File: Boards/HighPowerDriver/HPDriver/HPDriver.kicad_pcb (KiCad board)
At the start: 4 copper layers, 100.6 x 76.2 mm, 143 parts, among them J1 60V_In, J2 USB_B_Mini, J3 Coils, J4 Screw_Terminal_01x06, J5 AVR-ISP-6, Q1 IRFR5410, Q10 IRF4950S, Q11 BC817, Q12 BC817, Q13 BC817, Q14 BC817, Q2 IRFR3910, Q3 IRFR3910, Q4 IRFR5410, Q5 IRFR5410, Q6 IRFR3910, Q7 IRFR3910, Q8 IRFR5410, Q9 BC817, SW1 SW_Push, U1 LM5009MM, U10 ATtiny2313A-SU, U11 74LVC1G125, U12 74LVC1G125, U13 74AHC1G00, U14 74LVC1G123, U2 TMC262, U3 FT230XS, U4 SFH6156, U5 SFH6156, U6 TLP118, U7 LTV-827S, U8 LTV-827S, U9 74HC14, X1 16MHz, Y1 20MHz

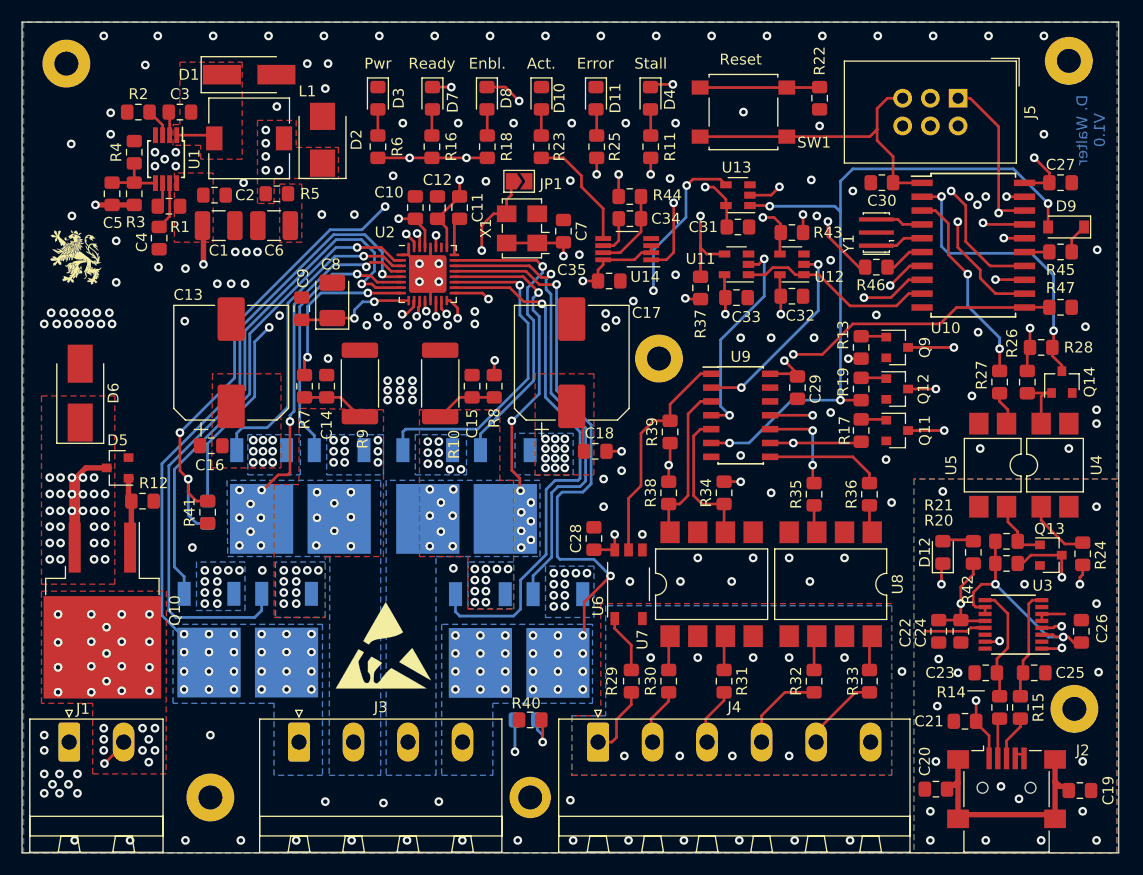
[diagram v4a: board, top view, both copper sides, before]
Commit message: Added Logic to allow local control of stepper trough µC
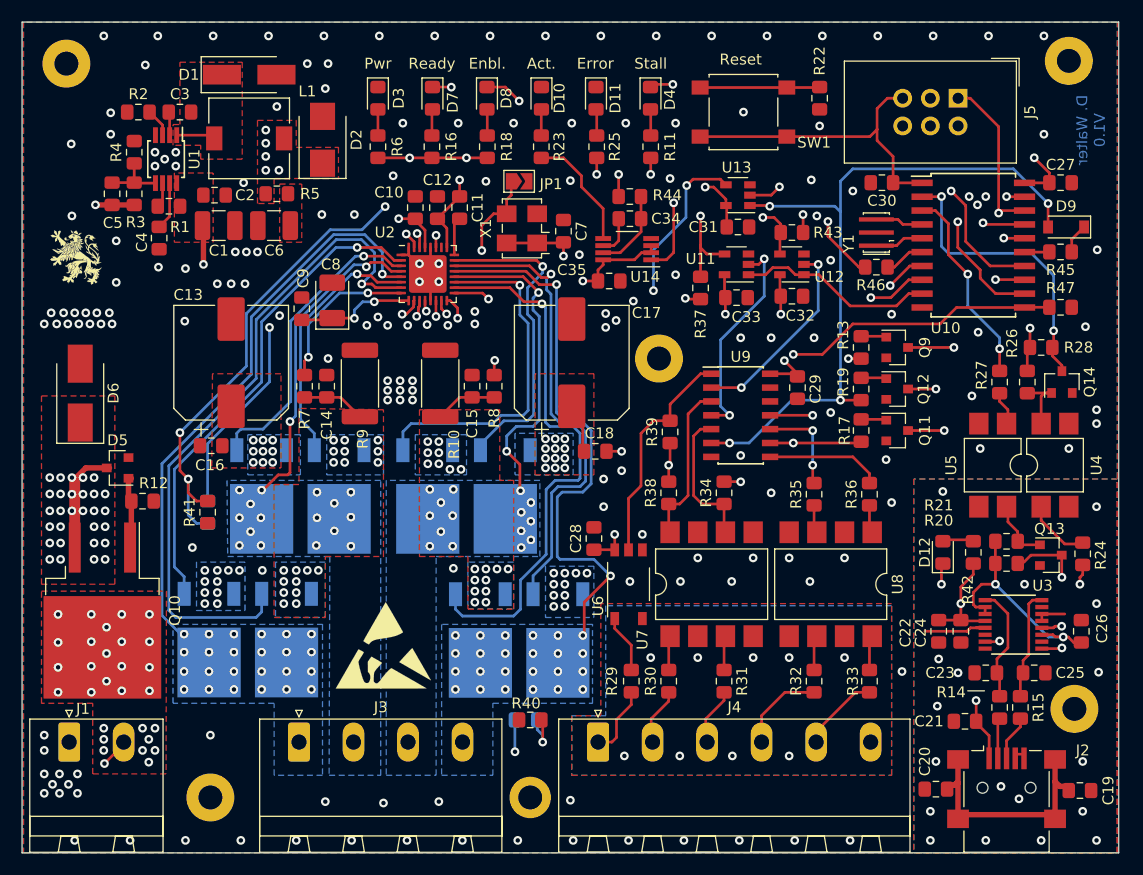
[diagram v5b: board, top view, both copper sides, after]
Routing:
- net Net-(Q7-Pad1): track 30.2 -> 31.9 mm
- net Net-(R43-Pad2): track 19.6 -> 17.9 mm
- net Net-(Q8-Pad1): track 28.0 -> 29.3 mm
- net Net-(Q1-Pad1): track 29.3 -> 28.0 mm
- net /Connector/Coil_B1: track 28.3 -> 29.6 mm
- net Net-(Q3-Pad1): track 49.6 -> 50.7 mm
- net Net-(Q2-Pad1): track 24.6 -> 23.5 mm
- net /Connector/Coil_A2: track 30.8 -> 29.7 mm
- net Net-(R7-Pad2): track 15.5 -> 14.5 mm
- net /Connector/Coil_B2: track 51.0 -> 51.9 mm
- net Net-(Q4-Pad1): track 43.7 -> 44.5 mm
- net Net-(C14-Pad1): track 6.61 -> 5.81 mm
- net +5V: track 92.8 -> 92.0 mm

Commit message: Changed Controller to ATtiny406
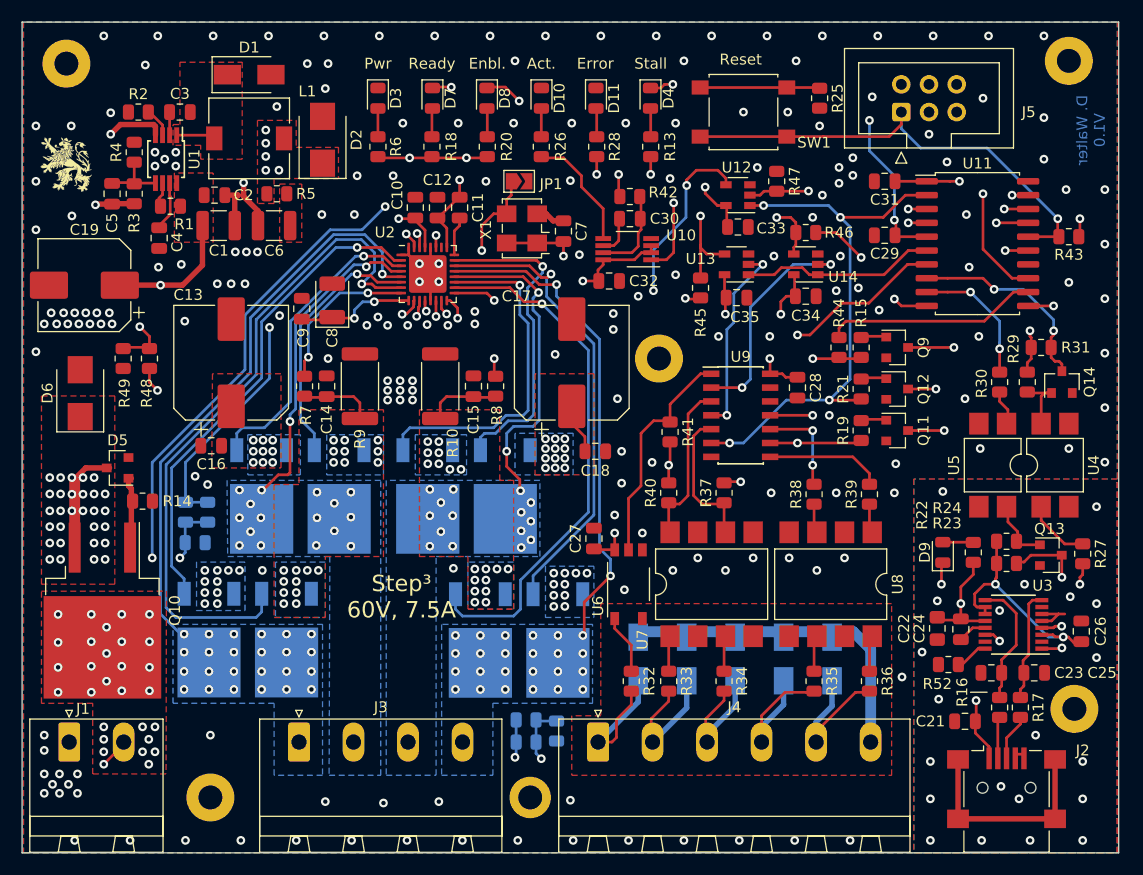
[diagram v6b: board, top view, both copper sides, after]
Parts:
- removed C20: 10nF, Capacitor_SMD:C_0805_2012Metric_Pad1.15x1.40mm_HandSolder
- removed the C30 at (163.2, 79.5)
- removed the D9 at (180.1, 83.6)
- removed the R45 at (179.6, 85.9)
- removed the REF** at (117.5, 121.9)
- removed the REF** at (99.7, 71.1)
- removed the U10 at (171.6, 85.2)
- removed Y1: 20MHz, Crystal:Resonator_SMD_muRata_CSTxExxV-3Pin_3.0x1.1mm_HandSoldering
- added C29: 470nF, Capacitor_SMD:C_0805_2012Metric, F.Cu at (163.4, 84.3)
- added D12: 13V, Diode_SMD:D_SMA, B.Cu at (140.8, 123.2)
- added D13: 13V, Diode_SMD:D_SMA, B.Cu at (145.3, 123.2)
- added D14: 13V, Diode_SMD:D_SMA, B.Cu at (149.7, 123.2)
- added D15: 13V, Diode_SMD:D_SMA, B.Cu at (154.2, 123.2)
- added D16: 13V, Diode_SMD:D_SMA, B.Cu at (158.6, 123.2)
- added R43: 10k, Resistor_SMD:R_0805_2012Metric, F.Cu at (180.3, 84.5)
- added R48: 10k, Resistor_SMD:R_0805_2012Metric, F.Cu at (96.0, 95.6)
- added R49: 750R, Resistor_SMD:R_0805_2012Metric, F.Cu at (93.6, 95.6)
- added R50: 39k, Resistor_SMD:R_0805_2012Metric, B.Cu at (99.3, 109.7)
- added R51: 39k, Resistor_SMD:R_0805_2012Metric, B.Cu at (130.6, 130.8)
- added R52: 1k, Resistor_SMD:R_0805_2012Metric, F.Cu at (169.3, 123.7)
- added U11: ATtiny406-S, Package_SO:SOIC-20W_7.5x12.8mm_P1.27mm, F.Cu at (172.0, 85.1)
- C1, C6: footprint Capacitor_SMD:C_1210_3225Metric_Pad1.42x2.65mm_HandSolder -> Capacitor_SMD:C_1210_3225Metric
- C10, C11, C12, C14, C15, C16, C18, C2, C21, C23, C24, C25, C26, C3, C4, C5, C7, C9: footprint Capacitor_SMD:C_0805_2012Metric_Pad1.15x1.40mm_HandSolder -> Capacitor_SMD:C_0805_2012Metric
- C19: value 10nF -> 47µF/100V; footprint Capacitor_SMD:C_0805_2012Metric_Pad1.15x1.40mm_HandSolder -> Capacitor_SMD:CP_Elec_8x10
- C27: renamed from C28; footprint Capacitor_SMD:C_0805_2012Metric_Pad1.15x1.40mm_HandSolder -> Capacitor_SMD:C_0805_2012Metric
- C28: renamed from C29; footprint Capacitor_SMD:C_0805_2012Metric_Pad1.15x1.40mm_HandSolder -> Capacitor_SMD:C_0805_2012Metric
- C30: renamed from C34; footprint Capacitor_SMD:C_0805_2012Metric_Pad1.15x1.40mm_HandSolder -> Capacitor_SMD:C_0805_2012Metric
- C31: renamed from C27; footprint Capacitor_SMD:C_0805_2012Metric_Pad1.15x1.40mm_HandSolder -> Capacitor_SMD:C_0805_2012Metric
- C32: renamed from C35; footprint Capacitor_SMD:C_0805_2012Metric_Pad1.15x1.40mm_HandSolder -> Capacitor_SMD:C_0805_2012Metric
- C33: renamed from C31; footprint Capacitor_SMD:C_0805_2012Metric_Pad1.15x1.40mm_HandSolder -> Capacitor_SMD:C_0805_2012Metric
- C34: renamed from C32; footprint Capacitor_SMD:C_0805_2012Metric_Pad1.15x1.40mm_HandSolder -> Capacitor_SMD:C_0805_2012Metric
- C35: renamed from C33; footprint Capacitor_SMD:C_0805_2012Metric_Pad1.15x1.40mm_HandSolder -> Capacitor_SMD:C_0805_2012Metric
- C8: footprint Capacitor_Tantalum_SMD:CP_EIA-3528-21_Kemet-B_Pad1.50x2.35mm_HandSolder -> Capacitor_Tantalum_SMD:CP_EIA-3528-21_Kemet-B
- D1: footprint Diode_SMD:D_SMA_Handsoldering -> Diode_SMD:D_SMA
- D10, D11, D3, D4, D7, D8: footprint LED_SMD:LED_0805_2012Metric_Pad1.15x1.40mm_HandSolder -> LED_SMD:LED_0805_2012Metric
- D6: value D_TVS -> 64V; footprint Diode_SMD:D_SMB_Handsoldering -> Diode_SMD:D_SMB
- D9: renamed from D12; footprint LED_SMD:LED_0805_2012Metric_Pad1.15x1.40mm_HandSolder -> LED_SMD:LED_0805_2012Metric
- J4: value Screw_Terminal_01x06 -> Control
- J5: value AVR-ISP-6 -> AVR-UPDI-6
- R1, R2, R3, R4, R47, R5, R6, R7, R8: footprint Resistor_SMD:R_0805_2012Metric_Pad1.15x1.40mm_HandSolder -> Resistor_SMD:R_0805_2012Metric
- R10, R9: footprint Resistor_SMD:R_2512_6332Metric_Pad1.40x3.35mm_HandSolder -> Resistor_SMD:R_2512_6332Metric
- R11: renamed from R40; value R -> 3k9; footprint Resistor_SMD:R_0805_2012Metric_Pad1.15x1.40mm_HandSolder -> Resistor_SMD:R_0805_2012Metric; moved to B.Cu
- R12: renamed from R41; value R -> 3k9; footprint Resistor_SMD:R_0805_2012Metric_Pad1.15x1.40mm_HandSolder -> Resistor_SMD:R_0805_2012Metric; moved to B.Cu
- R13: renamed from R11; footprint Resistor_SMD:R_0805_2012Metric_Pad1.15x1.40mm_HandSolder -> Resistor_SMD:R_0805_2012Metric
- R14: renamed from R12; footprint Resistor_SMD:R_0805_2012Metric_Pad1.15x1.40mm_HandSolder -> Resistor_SMD:R_0805_2012Metric
- R15: renamed from R13; footprint Resistor_SMD:R_0805_2012Metric_Pad1.15x1.40mm_HandSolder -> Resistor_SMD:R_0805_2012Metric
- R16: renamed from R14; footprint Resistor_SMD:R_0805_2012Metric_Pad1.15x1.40mm_HandSolder -> Resistor_SMD:R_0805_2012Metric
- R17: renamed from R15; footprint Resistor_SMD:R_0805_2012Metric_Pad1.15x1.40mm_HandSolder -> Resistor_SMD:R_0805_2012Metric
- R18: renamed from R16; footprint Resistor_SMD:R_0805_2012Metric_Pad1.15x1.40mm_HandSolder -> Resistor_SMD:R_0805_2012Metric
- R19: renamed from R17; footprint Resistor_SMD:R_0805_2012Metric_Pad1.15x1.40mm_HandSolder -> Resistor_SMD:R_0805_2012Metric
- R20: renamed from R18; footprint Resistor_SMD:R_0805_2012Metric_Pad1.15x1.40mm_HandSolder -> Resistor_SMD:R_0805_2012Metric
- R21: renamed from R19; footprint Resistor_SMD:R_0805_2012Metric_Pad1.15x1.40mm_HandSolder -> Resistor_SMD:R_0805_2012Metric
- R22: renamed from R42; footprint Resistor_SMD:R_0805_2012Metric_Pad1.15x1.40mm_HandSolder -> Resistor_SMD:R_0805_2012Metric
- R23: renamed from R20; footprint Resistor_SMD:R_0805_2012Metric_Pad1.15x1.40mm_HandSolder -> Resistor_SMD:R_0805_2012Metric
- R24: renamed from R21; footprint Resistor_SMD:R_0805_2012Metric_Pad1.15x1.40mm_HandSolder -> Resistor_SMD:R_0805_2012Metric
- R25: renamed from R22; value 1k -> 330R; footprint Resistor_SMD:R_0805_2012Metric_Pad1.15x1.40mm_HandSolder -> Resistor_SMD:R_0805_2012Metric
- R26: renamed from R23; footprint Resistor_SMD:R_0805_2012Metric_Pad1.15x1.40mm_HandSolder -> Resistor_SMD:R_0805_2012Metric
- R27: renamed from R24; value 380R -> 200R; footprint Resistor_SMD:R_0805_2012Metric_Pad1.15x1.40mm_HandSolder -> Resistor_SMD:R_0805_2012Metric
- R28: renamed from R25; footprint Resistor_SMD:R_0805_2012Metric_Pad1.15x1.40mm_HandSolder -> Resistor_SMD:R_0805_2012Metric
- R29: renamed from R26; footprint Resistor_SMD:R_0805_2012Metric_Pad1.15x1.40mm_HandSolder -> Resistor_SMD:R_0805_2012Metric
- R30: renamed from R27; value 380R -> 200R; footprint Resistor_SMD:R_0805_2012Metric_Pad1.15x1.40mm_HandSolder -> Resistor_SMD:R_0805_2012Metric
- R31: renamed from R28; footprint Resistor_SMD:R_0805_2012Metric_Pad1.15x1.40mm_HandSolder -> Resistor_SMD:R_0805_2012Metric
- R32: renamed from R29; value 270R -> 470R; footprint Resistor_SMD:R_0805_2012Metric_Pad1.15x1.40mm_HandSolder -> Resistor_SMD:R_0805_2012Metric
- R33: renamed from R30; value 200R -> 510R; footprint Resistor_SMD:R_0805_2012Metric_Pad1.15x1.40mm_HandSolder -> Resistor_SMD:R_0805_2012Metric
- R34: renamed from R31; value 200R -> 510R; footprint Resistor_SMD:R_0805_2012Metric_Pad1.15x1.40mm_HandSolder -> Resistor_SMD:R_0805_2012Metric
- R35: renamed from R32; value 200R -> 430R; footprint Resistor_SMD:R_0805_2012Metric_Pad1.15x1.40mm_HandSolder -> Resistor_SMD:R_0805_2012Metric
- R36: renamed from R33; value 200R -> 430R; footprint Resistor_SMD:R_0805_2012Metric_Pad1.15x1.40mm_HandSolder -> Resistor_SMD:R_0805_2012Metric
- R37: renamed from R34; footprint Resistor_SMD:R_0805_2012Metric_Pad1.15x1.40mm_HandSolder -> Resistor_SMD:R_0805_2012Metric
- R38: renamed from R35; footprint Resistor_SMD:R_0805_2012Metric_Pad1.15x1.40mm_HandSolder -> Resistor_SMD:R_0805_2012Metric
- R39: renamed from R36; footprint Resistor_SMD:R_0805_2012Metric_Pad1.15x1.40mm_HandSolder -> Resistor_SMD:R_0805_2012Metric
- R40: renamed from R38; footprint Resistor_SMD:R_0805_2012Metric_Pad1.15x1.40mm_HandSolder -> Resistor_SMD:R_0805_2012Metric
- R41: renamed from R39; footprint Resistor_SMD:R_0805_2012Metric_Pad1.15x1.40mm_HandSolder -> Resistor_SMD:R_0805_2012Metric
- R42: renamed from R44; footprint Resistor_SMD:R_0805_2012Metric_Pad1.15x1.40mm_HandSolder -> Resistor_SMD:R_0805_2012Metric
- R44: renamed from R46; footprint Resistor_SMD:R_0805_2012Metric_Pad1.15x1.40mm_HandSolder -> Resistor_SMD:R_0805_2012Metric
- R45: renamed from R37; footprint Resistor_SMD:R_0805_2012Metric_Pad1.15x1.40mm_HandSolder -> Resistor_SMD:R_0805_2012Metric
- R46: renamed from R43; footprint Resistor_SMD:R_0805_2012Metric_Pad1.15x1.40mm_HandSolder -> Resistor_SMD:R_0805_2012Metric
- TH1, TH2: value Thermistor_NTC -> 10k; footprint Resistor_SMD:R_0805_2012Metric_Pad1.15x1.40mm_HandSolder -> Resistor_SMD:R_0805_2012Metric
- moved C19 102.4 mm to (90.0, 88.9), turned to 180 degrees
- moved R47 28.5 mm to (153.5, 79.4), turned to 270 degrees
- moved C31 16.1 mm to (163.4, 79.4), turned to 180 degrees
- moved G*** 8.56 mm to (88.4, 77.9)
- moved R44 8.13 mm to (159.3, 94.6), turned to 90 degrees
- moved J5 5.36 mm to (165.0, 73.0), turned to 90 degrees
- moved R12 3.02 mm to (100.2, 112.5), turned to 0 degrees
- moved R11 2.62 mm to (133.3, 129.8), turned to 270 degrees
- moved C34 1.27 mm to (156.2, 89.9)
- moved R46 1.27 mm to (156.2, 84.1)
- moved U14 1.27 mm to (156.2, 87.0)
- moved C23 0.51 mm to (173.2, 124.5)
- moved C22 0.29 mm to (168.3, 120.4)
- moved R10 0.25 mm to (122.7, 98.2)
- moved R9 0.25 mm to (115.3, 98.2)
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- renumbered U14 to U10, U13 to U12, U11 to U13, U12 to U14
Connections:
- C19 pad 1: Net-(C19-Pad1) -> +48V
- C19 pad 2: GNDS -> GND
- D9 pad 1: Net-(D12-Pad1) (its old number) -> Net-(D9-Pad1)
- J2 pad 6: Net-(C19-Pad1) -> Net-(J2-Pad6)
- J5 pad 1: /Controller/MISO -> /Connector/Reset
- J5 pad 3: /Controller/SCK -> (no net)
- J5 pad 4: /Controller/MOSI -> (no net)
- J5 pad 5: /Connector/Reset -> (no net)
- U3 pad 14: (no net) -> Net-(D9-Pad1)
- U3 pad 15: Net-(D12-Pad1) (its old number) -> (no net)
- U3 pad 16: (no net) -> Net-(R52-Pad1)
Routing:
- net /Connector/VSup: track 0.00 -> 107.9 mm, vias 0 -> 3
- net GNDA: track 0.00 -> 30.5 mm, vias 9 -> 0
- net Net-(C19-Pad1): track 22.4 -> 0.00 mm
- net Net-(J2-Pad6): track 0.00 -> 19.8 mm
- net /Connector/Enable: track 67.0 -> 50.8 mm
- net Net-(R44-Pad2): track 3.74 -> 19.5 mm
- net GND: track 10.4 -> 25.6 mm, vias 169 -> 191
- net /Connector/Reset: track 29.3 -> 43.7 mm, vias 0 -> 1
- net /Controller/SCK: track 78.6 -> 66.0 mm
- net Net-(D12-Pad1) (its old number): track 11.8 -> 0.00 mm, vias 2 -> 0
- net /Controller/MISO: track 78.2 -> 66.6 mm
- net /Controller/MOSI: track 77.7 -> 66.2 mm
- net +48V: track 83.0 -> 93.8 mm, vias 72 -> 73
- net Net-(D9-Pad1): track 2.87 -> 12.1 mm, vias 0 -> 2
- net Net-(R46-Pad2): track 17.9 -> 26.8 mm
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- removed copper zone on B.Cu, net GNDA
- removed copper zone on In2.Cu, net GNDA
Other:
- board text added: "5-12V"
- board text added: "Step³ 60V, 7.5A"
- board text removed: "Isolated"

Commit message: Moved to Kicad 6.0
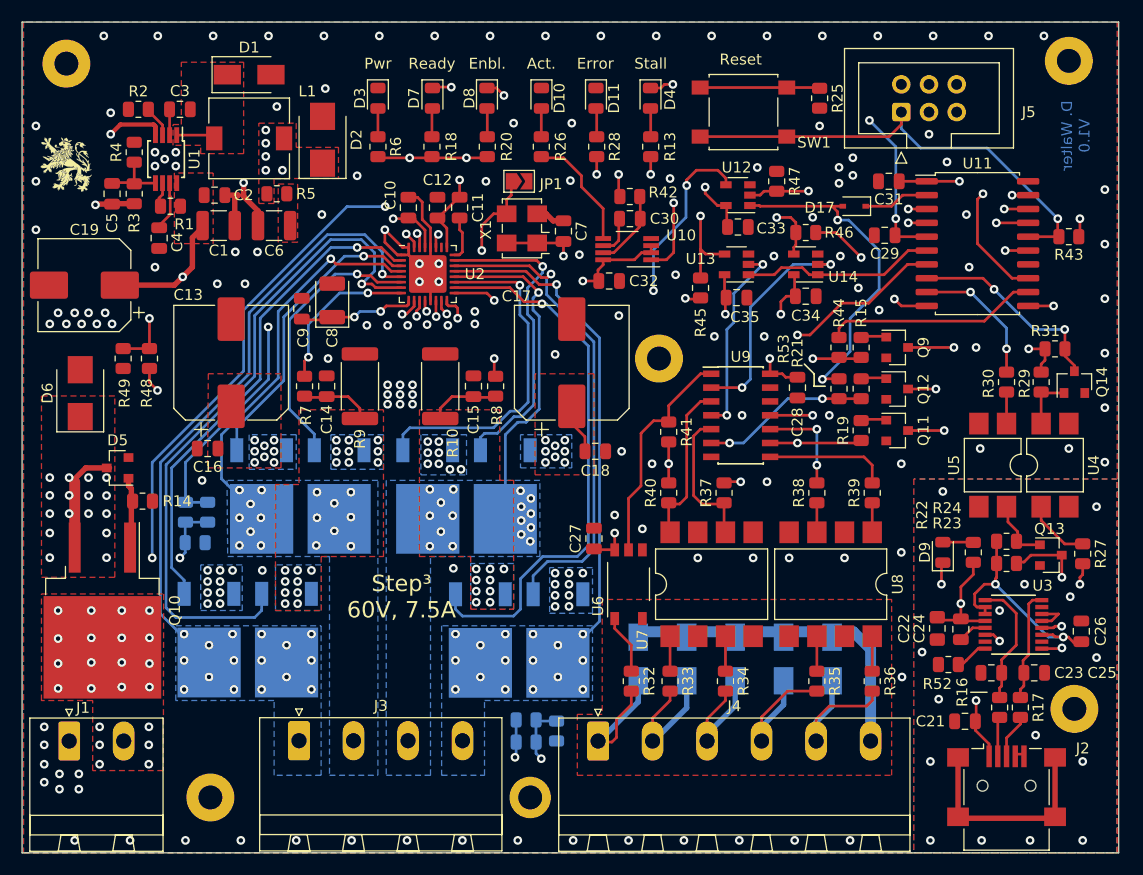
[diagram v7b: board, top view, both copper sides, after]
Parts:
- added D17: B0540WS-7 DII, Diode_SMD:D_SOD-323, F.Cu at (160.7, 81.7)
- added R53: 270R, Resistor_SMD:R_0805_2012Metric, F.Cu at (159.3, 98.4)
- moved R31 1.28 mm to (179.1, 94.7)
- moved R29 1.27 mm to (177.8, 97.8)
- moved Q14 1.14 mm to (180.8, 97.8)
- moved C10 0.64 mm to (119.8, 81.8)
- moved R30 0.63 mm to (174.6, 97.8)
- moved C16 0.41 mm to (101.3, 103.9)
- moved C31 0.38 mm to (163.8, 79.4)
- moved R39 0.28 mm to (162.3, 108.0)
- moved R38 0.28 mm to (157.2, 108.0)
- moved R36 0.25 mm to (162.3, 125.2)
- moved C3 0.25 mm to (98.8, 72.8)
- moved R2 0.25 mm to (95.0, 72.8)
- moved R35 0.25 mm to (157.2, 125.2)
- moved J2 0.19 mm to (174.6, 134.8)
- moved J3 0.13 mm to (109.7, 130.7)
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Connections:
- net /Connector/Ready renamed /Controller/Ready_Ctrler
- net /Driver/Dir renamed /Controller/Dir_TMC
- net /Driver/DriveEN renamed /Controller/Drive_EN
- net /Driver/Step renamed /Controller/Step_TMC
- net Net-(R45-Pad2) renamed /Controller/Dir_Local
- net Net-(R46-Pad2) renamed /Controller/Step_Local
- J2 pad 6: Net-(J2-Pad6) -> unconnected-(J2-Pad6)
- J5 pad 3: (no net) -> unconnected-(J5-Pad3)
- J5 pad 4: (no net) -> unconnected-(J5-Pad4)
- J5 pad 5: (no net) -> unconnected-(J5-Pad5)
- U11 pad 14: (no net) -> unconnected-(U11-Pad14)
- U11 pad 2: /Connector/Enable -> /Controller/Enable_Ctrlr
- U12 pad 1: /Connector/Enable -> Net-(D17-Pad2)
- U2 pad 26: (no net) -> unconnected-(U2-Pad26)
- U3 pad 15: (no net) -> unconnected-(U3-Pad15)
- U3 pad 2: (no net) -> unconnected-(U3-Pad2)
- U3 pad 7: (no net) -> unconnected-(U3-Pad7)
- U9 pad 12: (no net) -> unconnected-(U9-Pad12)
- U9 pad 13: (no net) -> unconnected-(U9-Pad13)
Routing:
- net /Connector/Enable: track 50.8 -> 15.4 mm, vias 4 -> 2
- net Net-(D17-Pad2): track 0.00 -> 30.5 mm, vias 0 -> 2
- net unconnected-(J2-Pad6): track 0.00 -> 19.8 mm
- net Net-(J2-Pad6): track 19.8 -> 0.00 mm
- net GND: track 25.6 -> 36.8 mm, vias 191 -> 140
- net /Connector/Coil_A2: track 29.7 -> 36.5 mm, vias 18 -> 17
- net /Controller/Enable_Ctrlr: track 0.00 -> 6.02 mm
- net /Connector/VSup: track 107.9 -> 112.3 mm
- net +48V: track 93.8 -> 90.2 mm, vias 73 -> 53
- net Net-(J1-Pad2): track 2.79 -> 0.00 mm, vias 29 -> 22
- net Net-(Q3-Pad1): track 48.9 -> 50.9 mm
- net Net-(Q4-Pad1): track 43.1 -> 44.9 mm
- net Net-(Q2-Pad1): track 23.5 -> 25.2 mm
- net /Connector/Coil_B1: track 29.8 -> 31.3 mm
- net +5V: track 99.8 -> 98.3 mm
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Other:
- net class Default removed
